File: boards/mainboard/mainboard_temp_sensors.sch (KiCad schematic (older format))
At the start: 1 part, among them J201 DB25_FEMALE

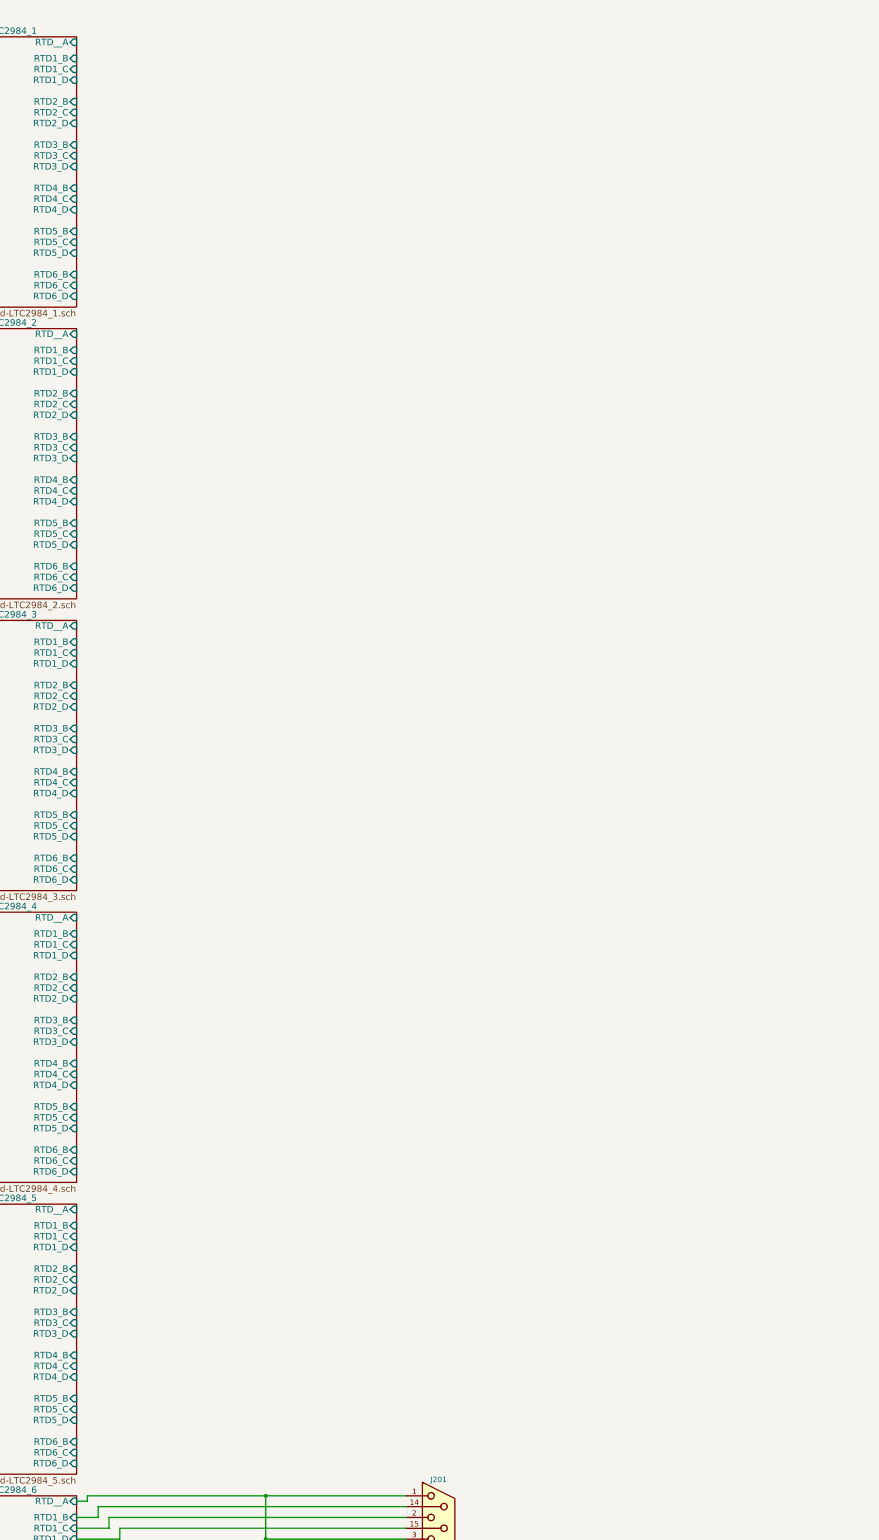
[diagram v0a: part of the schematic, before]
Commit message: [mainboard] add D-Sub HD 44 and 78 lib, wire PT-100 connectors
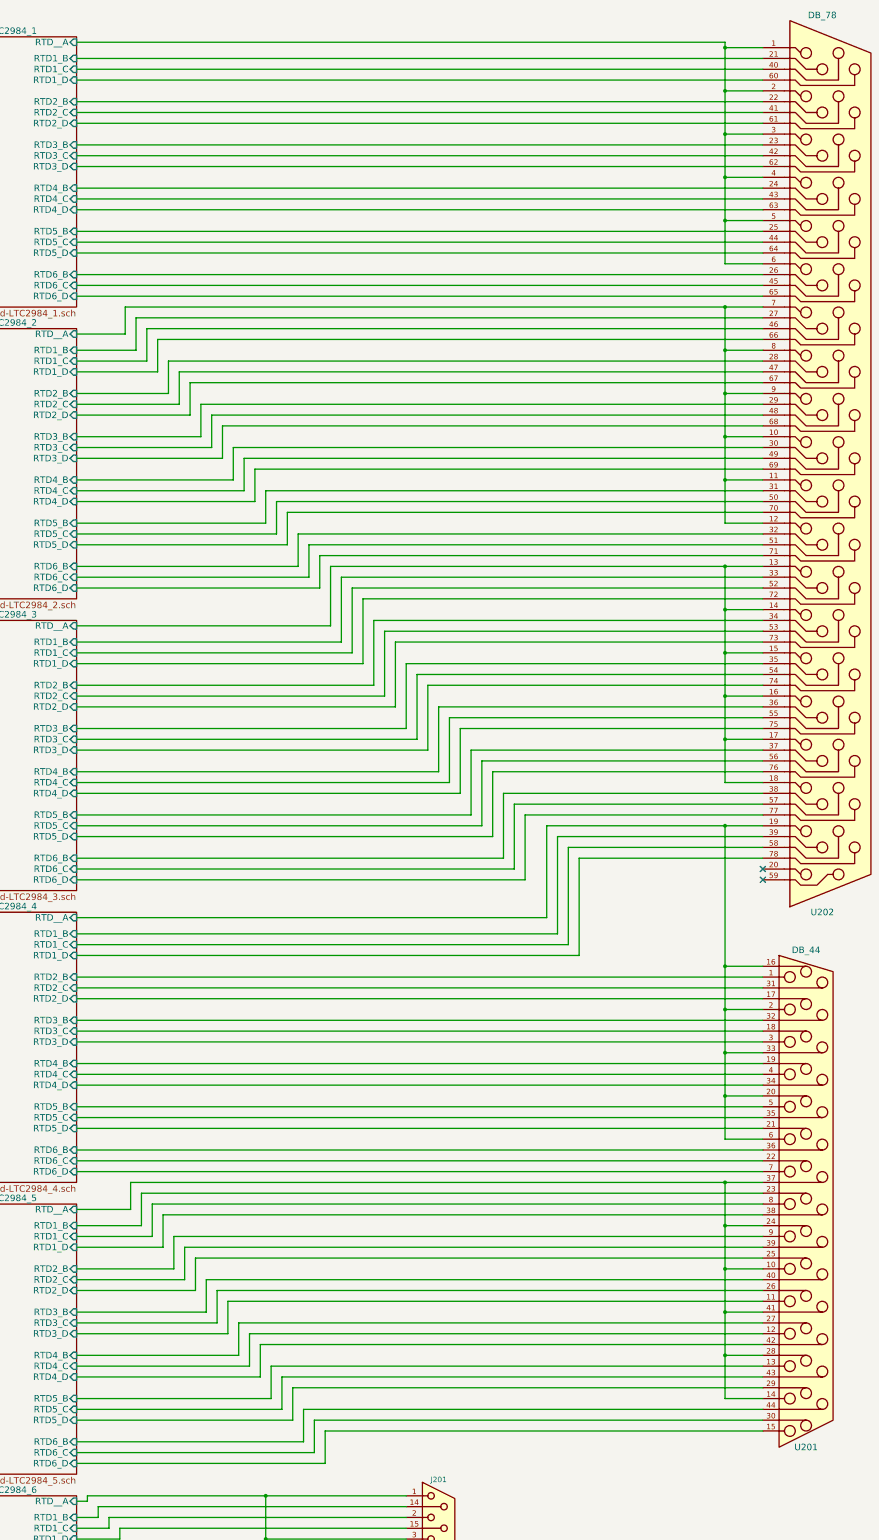
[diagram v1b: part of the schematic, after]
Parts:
- added U201: DB_44, symbol DB_44
- added U202: DB_78, symbol DB_78
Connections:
- net Mainboard_LTC2984_1/RTD1_B: now also U202.21
- net Mainboard_LTC2984_1/RTD1_C: now also U202.40
- net Mainboard_LTC2984_1/RTD1_D: now also U202.60
- net Mainboard_LTC2984_1/RTD2_B: now also U202.22
- net Mainboard_LTC2984_1/RTD2_C: now also U202.41
- net Mainboard_LTC2984_1/RTD2_D: now also U202.61
- net Mainboard_LTC2984_1/RTD3_B: now also U202.23
- net Mainboard_LTC2984_1/RTD3_C: now also U202.42
- net Mainboard_LTC2984_1/RTD3_D: now also U202.62
- net Mainboard_LTC2984_1/RTD4_B: now also U202.24
- net Mainboard_LTC2984_1/RTD4_C: now also U202.43
- net Mainboard_LTC2984_1/RTD4_D: now also U202.63
- net Mainboard_LTC2984_1/RTD5_B: now also U202.25
- net Mainboard_LTC2984_1/RTD5_C: now also U202.44
- net Mainboard_LTC2984_1/RTD5_D: now also U202.64
- net Mainboard_LTC2984_1/RTD6_B: now also U202.26
- net Mainboard_LTC2984_1/RTD6_C: now also U202.45
- net Mainboard_LTC2984_1/RTD6_D: now also U202.65
- net Mainboard_LTC2984_1/RTD__A: now also U202.1, U202.2, U202.3, U202.4, U202.5, U202.6
- net Mainboard_LTC2984_2/RTD1_B: now also U202.27
- net Mainboard_LTC2984_2/RTD1_C: now also U202.46
- net Mainboard_LTC2984_2/RTD1_D: now also U202.66
- net Mainboard_LTC2984_2/RTD2_B: now also U202.28
- net Mainboard_LTC2984_2/RTD2_C: now also U202.47
- net Mainboard_LTC2984_2/RTD2_D: now also U202.67
- net Mainboard_LTC2984_2/RTD3_B: now also U202.29
- net Mainboard_LTC2984_2/RTD3_C: now also U202.48
- net Mainboard_LTC2984_2/RTD3_D: now also U202.68
- net Mainboard_LTC2984_2/RTD4_B: now also U202.30
- net Mainboard_LTC2984_2/RTD4_C: now also U202.49
- net Mainboard_LTC2984_2/RTD4_D: now also U202.69
- net Mainboard_LTC2984_2/RTD5_B: now also U202.31
- net Mainboard_LTC2984_2/RTD5_C: now also U202.50
- net Mainboard_LTC2984_2/RTD5_D: now also U202.70
- net Mainboard_LTC2984_2/RTD6_B: now also U202.32
- net Mainboard_LTC2984_2/RTD6_C: now also U202.51
- net Mainboard_LTC2984_2/RTD6_D: now also U202.71
- net Mainboard_LTC2984_2/RTD__A: now also U202.10, U202.11, U202.12, U202.7, U202.8, U202.9
- net Mainboard_LTC2984_3/RTD1_B: now also U202.33
- net Mainboard_LTC2984_3/RTD1_C: now also U202.52
- net Mainboard_LTC2984_3/RTD1_D: now also U202.72
- net Mainboard_LTC2984_3/RTD2_B: now also U202.34
- net Mainboard_LTC2984_3/RTD2_C: now also U202.53
- net Mainboard_LTC2984_3/RTD2_D: now also U202.73
- net Mainboard_LTC2984_3/RTD3_B: now also U202.35
- net Mainboard_LTC2984_3/RTD3_C: now also U202.54
- net Mainboard_LTC2984_3/RTD3_D: now also U202.74
- net Mainboard_LTC2984_3/RTD4_B: now also U202.36
- net Mainboard_LTC2984_3/RTD4_C: now also U202.55
- net Mainboard_LTC2984_3/RTD4_D: now also U202.75
- net Mainboard_LTC2984_3/RTD5_B: now also U202.37
- net Mainboard_LTC2984_3/RTD5_C: now also U202.56
- net Mainboard_LTC2984_3/RTD5_D: now also U202.76
- net Mainboard_LTC2984_3/RTD6_B: now also U202.38
- net Mainboard_LTC2984_3/RTD6_C: now also U202.57
- net Mainboard_LTC2984_3/RTD6_D: now also U202.77
- net Mainboard_LTC2984_3/RTD__A: now also U202.13, U202.14, U202.15, U202.16, U202.17, U202.18
- net Mainboard_LTC2984_4/RTD1_B: now also U202.39
- net Mainboard_LTC2984_4/RTD1_C: now also U202.58
- net Mainboard_LTC2984_4/RTD1_D: now also U202.78
- net Mainboard_LTC2984_4/RTD2_B: now also U201.1
- net Mainboard_LTC2984_4/RTD2_C: now also U201.31
- net Mainboard_LTC2984_4/RTD2_D: now also U201.17
- net Mainboard_LTC2984_4/RTD3_B: now also U201.32
- net Mainboard_LTC2984_4/RTD3_C: now also U201.18
- net Mainboard_LTC2984_4/RTD3_D: now also U201.3
- net Mainboard_LTC2984_4/RTD4_B: now also U201.19
- net Mainboard_LTC2984_4/RTD4_C: now also U201.4
- net Mainboard_LTC2984_4/RTD4_D: now also U201.34
- net Mainboard_LTC2984_4/RTD5_B: now also U201.5
- net Mainboard_LTC2984_4/RTD5_C: now also U201.35
- net Mainboard_LTC2984_4/RTD5_D: now also U201.21
- net Mainboard_LTC2984_4/RTD6_B: now also U201.36
- net Mainboard_LTC2984_4/RTD6_C: now also U201.22
- net Mainboard_LTC2984_4/RTD6_D: now also U201.7
- net Mainboard_LTC2984_4/RTD__A: now also U201.16, U201.2, U201.20, U201.33, U201.6, U202.19
- net Mainboard_LTC2984_5/RTD1_B: now also U201.23
- net Mainboard_LTC2984_5/RTD1_C: now also U201.8
- net Mainboard_LTC2984_5/RTD1_D: now also U201.38
- net Mainboard_LTC2984_5/RTD2_B: now also U201.9
- net Mainboard_LTC2984_5/RTD2_C: now also U201.39
- net Mainboard_LTC2984_5/RTD2_D: now also U201.25
- net Mainboard_LTC2984_5/RTD3_B: now also U201.40
- net Mainboard_LTC2984_5/RTD3_C: now also U201.26
- net Mainboard_LTC2984_5/RTD3_D: now also U201.11
- net Mainboard_LTC2984_5/RTD4_B: now also U201.27
- net Mainboard_LTC2984_5/RTD4_C: now also U201.12
- net Mainboard_LTC2984_5/RTD4_D: now also U201.42
- net Mainboard_LTC2984_5/RTD5_B: now also U201.13
- net Mainboard_LTC2984_5/RTD5_C: now also U201.43
- net Mainboard_LTC2984_5/RTD5_D: now also U201.29
- net Mainboard_LTC2984_5/RTD6_B: now also U201.44
- net Mainboard_LTC2984_5/RTD6_C: now also U201.30
- net Mainboard_LTC2984_5/RTD6_D: now also U201.15
- net Mainboard_LTC2984_5/RTD__A: now also U201.10, U201.14, U201.24, U201.28, U201.37, U201.41
- no-connect marks 0 -> 2

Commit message: [mainboard] update connectors, select most footprints; docs: update SVGs
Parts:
- J201: value DB25_FEMALE -> RTD_31-36
- U201: value DB_44 -> RTD_20-30
- U202: value DB_78 -> RTD_1-19
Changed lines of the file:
@@
 Title "Mainboard Temperature Measurement Systems"
 Date "2017-04-19"
-Rev "11"
+Rev "12"
 Comp "VIPER"
 Comment1 ""
@@
 $EndSheet
 $Comp
-L DB25_FEMALE J201
-U 1 1 58FE1FD8
-P 7200 15600
-F 0 "J201" H 7200 16950 50  0000 C CNN
-F 1 "DB25_FEMALE" H 7200 14225 50  0000 C CNN
-F 2 "" H 7200 15600 50  0001 C CNN
-F 3 "" H 7200 15600 50  0001 C CNN
-	1    7200 15600
-	1    0    0    -1
-$EndComp
-$Comp
-L GND #PWR201
+L GND #PWR016
 U 1 1 58FE6256
 P 6800 16900
-F 0 "#PWR201" H 6800 16650 50  0001 C CNN
+F 0 "#PWR016" H 6800 16650 50  0001 C CNN
 F 1 "GND" H 6800 16750 50  0000 C CNN
 F 2 "" H 6800 16900 50  0001 C CNN
@@
 	1    0    0    -1
 $EndComp
-Wire Wire Line
-	6800 16900 6800 15600
-Wire Wire Line
-	6800 15600 6900 15600
-Wire Wire Line
-	3850 16800 6900 16800
-Wire Wire Line
-	3850 16700 6900 16700
-Wire Wire Line
-	3850 16600 6900 16600
-Wire Wire Line
-	3850 16400 6900 16400
-Wire Wire Line
-	3850 16300 6900 16300
-Wire Wire Line
-	6900 16200 3850 16200
-Wire Wire Line
-	3850 16000 6900 16000
-Wire Wire Line
-	6900 15900 3850 15900
-Wire Wire Line
-	3850 15800 6900 15800
-Wire Wire Line
-	3850 14600 4050 14600
-Wire Wire Line
-	4050 14600 4050 14500
-Wire Wire Line
-	4050 14500 6900 14500
-Wire Wire Line
-	6900 14600 4150 14600
-Wire Wire Line
-	4150 14600 4150 14700
-Wire Wire Line
-	4150 14700 3850 14700
-Wire Wire Line
-	3850 14800 4250 14800
-Wire Wire Line
-	4250 14800 4250 14700
-Wire Wire Line
-	4250 14700 6900 14700
-Wire Wire Line
-	6900 14900 4050 14900
-Wire Wire Line
-	4050 14900 4050 15000
-Wire Wire Line
-	4050 15000 3850 15000
-Wire Wire Line
-	3850 15100 4150 15100
-Wire Wire Line
-	4150 15100 4150 15000
-Wire Wire Line
-	4150 15000 6900 15000
-Wire Wire Line
-	6900 15100 4250 15100
-Wire Wire Line
-	4250 15100 4250 15200
-Wire Wire Line
-	4250 15200 3850 15200
-Wire Wire Line
-	3850 15400 4050 15400
-Wire Wire Line
-	4050 15400 4050 15300
-Wire Wire Line
-	4050 15300 6900 15300
-Wire Wire Line
-	6900 15400 4150 15400
-Wire Wire Line
-	4150 15400 4150 15500
-Wire Wire Line
-	4150 15500 3850 15500
-Wire Wire Line
-	3850 15600 4250 15600
-Wire Wire Line
-	4250 15600 4250 15500
-Wire Wire Line
-	4250 15500 6900 15500
-Wire Wire Line
-	3850 14450 3950 14450
-Wire Wire Line
-	3950 14450 3950 14400
-Wire Wire Line
-	3950 14400 6900 14400
-Wire Wire Line
-	5600 14400 5600 16500
-Wire Wire Line
-	5600 14800 6900 14800
-Connection ~ 5600 14400
-Wire Wire Line
-	5600 15200 6900 15200
-Connection ~ 5600 14800
-Wire Wire Line
-	5600 15700 6900 15700
-Connection ~ 5600 15200
-Wire Wire Line
-	5600 16100 6900 16100
-Connection ~ 5600 15700
-Wire Wire Line
-	5600 16500 6900 16500
-Connection ~ 5600 16100
-Wire Wire Line
-	1350 9200 2550 9200
-Wire Wire Line
-	1750 11900 2550 11900
-Connection ~ 1750 9200
-Wire Wire Line
-	1350 9300 2550 9300
-Wire Wire Line
-	2550 9400 1350 9400
-Wire Wire Line
-	1650 9300 1650 14700
-Wire Wire Line
-	1650 12000 2550 12000
-Connection ~ 1650 9300
-Wire Wire Line
-	2550 12100 1550 12100
-Wire Wire Line
-	1550 9400 1550 14800
-Connection ~ 1550 9400
-Wire Wire Line
-	1550 14800 2550 14800
-Connection ~ 1550 12100
-Wire Wire Line
-	1650 14700 2550 14700
-Connection ~ 1650 12000
-Wire Wire Line
-	1750 14600 2550 14600
-Connection ~ 1750 11900
-Wire Wire Line
-	2550 14500 2450 14500
-Wire Wire Line
-	2550 14900 2450 14900
-Wire Wire Line
-	2550 11800 2450 11800
-Wire Wire Line
-	2450 12200 2550 12200
-Wire Wire Line
-	1350 1100 2550 1100
-Wire Wire Line
-	2550 1200 1350 1200
-Wire Wire Line
-	1350 1300 2550 1300
-Wire Wire Line
-	2550 1400 2450 1400
-Wire Wire Line
-	2450 1000 2550 1000
-Wire Wire Line
-	1650 1200 1650 6600
-Wire Wire Line
-	1650 3900 2550 3900
-Connection ~ 1650 1200
-Wire Wire Line
-	2550 4000 1550 4000
-Wire Wire Line
-	1550 1300 1550 6700
-Connection ~ 1550 1300
-Wire Wire Line
-	1750 1100 1750 6500
-Wire Wire Line
-	1750 3800 2550 3800
-Connection ~ 1750 1100
-Wire Wire Line
-	2550 3700 2450 3700
-Wire Wire Line
-	2450 4100 2550 4100
-Wire Wire Line
-	1550 6700 2550 6700
-Connection ~ 1550 4000
-Wire Wire Line
-	1650 6600 2550 6600
-Connection ~ 1650 3900
-Wire Wire Line
-	1750 6500 2550 6500
-Connection ~ 1750 3800
-Wire Wire Line
-	2550 6400 2450 6400
-Wire Wire Line
-	2450 6800 2550 6800
-Wire Wire Line
-	2550 9500 2450 9500
-Wire Wire Line
-	2450 9100 2550 9100
-Wire Wire Line
-	1750 9200 1750 14600
 $Comp
 L DB_44 U201
@@
 P 10600 11600
 F 0 "U201" H 10600 9250 60  0000 C CNN
-F 1 "DB_44" H 10600 13850 60  0000 C CNN
+F 1 "RTD_20-30" H 10600 13850 60  0000 C CNN
 F 2 "" H 11800 11600 60  0001 C CNN
 F 3 "" H 11800 11600 60  0001 C CNN
@@
 P 10750 4700
 F 0 "U202" H 10750 400 60  0000 C CNN
-F 1 "DB_78" H 10750 8700 60  0000 C CNN
+F 1 "RTD_1-19" H 10750 8700 60  0000 C CNN
 F 2 "" H 10600 8400 60  0001 C CNN
 F 3 "" H 10600 8400 60  0001 C CNN
@@
 	1    0    0    -1
 $EndComp
+NoConn ~ 10200 8600
+NoConn ~ 10200 8700
+$Comp
+L DB25_FEMALE J201
+U 1 1 58FE1FD8
+P 7200 15600
+F 0 "J201" H 7200 16950 50  0000 C CNN
+F 1 "RTD_31-36" H 7200 14225 50  0000 C CNN
+F 2 "" H 7200 15600 50  0001 C CNN
+F 3 "" H 7200 15600 50  0001 C CNN
+	1    7200 15600
+	1    0    0    -1
+$EndComp
+Wire Wire Line
+	6800 16900 6800 15600
+Wire Wire Line
+	6800 15600 6900 15600
+Wire Wire Line
+	3850 16800 6900 16800
+Wire Wire Line
+	3850 16700 6900 16700
+Wire Wire Line
+	3850 16600 6900 16600
+Wire Wire Line
+	3850 16400 6900 16400
+Wire Wire Line
+	3850 16300 6900 16300
+Wire Wire Line
+	6900 16200 3850 16200
+Wire Wire Line
+	3850 16000 6900 16000
+Wire Wire Line
+	6900 15900 3850 15900
+Wire Wire Line
+	3850 15800 6900 15800
+Wire Wire Line
+	3850 14600 4050 14600
+Wire Wire Line
+	4050 14600 4050 14500
+Wire Wire Line
+	4050 14500 6900 14500
+Wire Wire Line
+	6900 14600 4150 14600
+Wire Wire Line
+	4150 14600 4150 14700
+Wire Wire Line
+	4150 14700 3850 14700
+Wire Wire Line
+	3850 14800 4250 14800
+Wire Wire Line
+	4250 14800 4250 14700
+Wire Wire Line
+	4250 14700 6900 14700
+Wire Wire Line
+	6900 14900 4050 14900
+Wire Wire Line
+	4050 14900 4050 15000
+Wire Wire Line
+	4050 15000 3850 15000
+Wire Wire Line
+	3850 15100 4150 15100
+Wire Wire Line
+	4150 15100 4150 15000
+Wire Wire Line
+	4150 15000 6900 15000
+Wire Wire Line
+	6900 15100 4250 15100
+Wire Wire Line
+	4250 15100 4250 15200
+Wire Wire Line
+	4250 15200 3850 15200
+Wire Wire Line
+	3850 15400 4050 15400
+Wire Wire Line
+	4050 15400 4050 15300
+Wire Wire Line
+	4050 15300 6900 15300
+Wire Wire Line
+	6900 15400 4150 15400
+Wire Wire Line
+	4150 15400 4150 15500
+Wire Wire Line
+	4150 15500 3850 15500
+Wire Wire Line
+	3850 15600 4250 15600
+Wire Wire Line
+	4250 15600 4250 15500
+Wire Wire Line
+	4250 15500 6900 15500
+Wire Wire Line
+	3850 14450 3950 14450
+Wire Wire Line
+	3950 14450 3950 14400
+Wire Wire Line
+	3950 14400 6900 14400
+Wire Wire Line
+	5600 14400 5600 16500
+Wire Wire Line
+	5600 14800 6900 14800
+Connection ~ 5600 14400
+Wire Wire Line
+	5600 15200 6900 15200
+Connection ~ 5600 14800
+Wire Wire Line
+	5600 15700 6900 15700
+Connection ~ 5600 15200
+Wire Wire Line
+	5600 16100 6900 16100
+Connection ~ 5600 15700
+Wire Wire Line
+	5600 16500 6900 16500
+Connection ~ 5600 16100
+Wire Wire Line
+	1350 9200 2550 9200
+Wire Wire Line
+	1750 11900 2550 11900
+Connection ~ 1750 9200
+Wire Wire Line
+	1350 9300 2550 9300
+Wire Wire Line
+	2550 9400 1350 9400
+Wire Wire Line
+	1650 9300 1650 14700
+Wire Wire Line
+	1650 12000 2550 12000
+Connection ~ 1650 9300
+Wire Wire Line
+	2550 12100 1550 12100
+Wire Wire Line
+	1550 9400 1550 14800
+Connection ~ 1550 9400
+Wire Wire Line
+	1550 14800 2550 14800
+Connection ~ 1550 12100
+Wire Wire Line
+	1650 14700 2550 14700
+Connection ~ 1650 12000
+Wire Wire Line
+	1750 14600 2550 14600
+Connection ~ 1750 11900
+Wire Wire Line
+	2550 14500 2450 14500
+Wire Wire Line
+	2550 14900 2450 14900
+Wire Wire Line
+	2550 11800 2450 11800
+Wire Wire Line
+	2450 12200 2550 12200
+Wire Wire Line
+	1350 1100 2550 1100
+Wire Wire Line
+	2550 1200 1350 1200
+Wire Wire Line
+	1350 1300 2550 1300
+Wire Wire Line
+	2550 1400 2450 1400
+Wire Wire Line
+	2450 1000 2550 1000
+Wire Wire Line
+	1650 1200 1650 6600
+Wire Wire Line
+	1650 3900 2550 3900
+Connection ~ 1650 1200
+Wire Wire Line
+	2550 4000 1550 4000
+Wire Wire Line
+	1550 1300 1550 6700
+Connection ~ 1550 1300
+Wire Wire Line
+	1750 1100 1750 6500
+Wire Wire Line
+	1750 3800 2550 3800
+Connection ~ 1750 1100
+Wire Wire Line
+	2550 3700 2450 3700
+Wire Wire Line
+	2450 4100 2550 4100
+Wire Wire Line
+	1550 6700 2550 6700
+Connection ~ 1550 4000
+Wire Wire Line
+	1650 6600 2550 6600
+Connection ~ 1650 3900
+Wire Wire Line
+	1750 6500 2550 6500
+Connection ~ 1750 3800
+Wire Wire Line
+	2550 6400 2450 6400
+Wire Wire Line
+	2450 6800 2550 6800
+Wire Wire Line
+	2550 9500 2450 9500
+Wire Wire Line
+	2450 9100 2550 9100
+Wire Wire Line
+	1750 9200 1750 14600
 Wire Wire Line
 	3850 1200 10200 1200
@@
 	9850 11900 10200 11900
 Connection ~ 9850 11900
-NoConn ~ 10200 8600
-NoConn ~ 10200 8700
 $EndSCHEMATC

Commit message: [mainboard] layout: footprints assigned, first placement
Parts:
- J201: footprint (none) -> Connectors:DB25FD
- U201: footprint (none) -> D-Sub-HD:D-Sub_HD_44_F
- U202: footprint (none) -> D-Sub-HD:D-Sub_HD_78_F
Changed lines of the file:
@@
 $EndSheet
 $Comp
-L GND #PWR016
+L GND #PWR014
 U 1 1 58FE6256
 P 6800 16900
-F 0 "#PWR016" H 6800 16650 50  0001 C CNN
+F 0 "#PWR014" H 6800 16650 50  0001 C CNN
 F 1 "GND" H 6800 16750 50  0000 C CNN
 F 2 "" H 6800 16900 50  0001 C CNN
@@
 F 0 "U201" H 10600 9250 60  0000 C CNN
 F 1 "RTD_20-30" H 10600 13850 60  0000 C CNN
-F 2 "" H 11800 11600 60  0001 C CNN
+F 2 "D-Sub-HD:D-Sub_HD_44_F" H 11800 11600 60  0001 C CNN
 F 3 "" H 11800 11600 60  0001 C CNN
 	1    10600 11600
@@
 F 0 "U202" H 10750 400 60  0000 C CNN
 F 1 "RTD_1-19" H 10750 8700 60  0000 C CNN
-F 2 "" H 10600 8400 60  0001 C CNN
+F 2 "D-Sub-HD:D-Sub_HD_78_F" H 10600 8400 60  0001 C CNN
 F 3 "" H 10600 8400 60  0001 C CNN
 	1    10750 4700
@@
 F 0 "J201" H 7200 16950 50  0000 C CNN
 F 1 "RTD_31-36" H 7200 14225 50  0000 C CNN
-F 2 "" H 7200 15600 50  0001 C CNN
+F 2 "Connectors:DB25FD" H 7200 15600 50  0001 C CNN
 F 3 "" H 7200 15600 50  0001 C CNN
 	1    7200 15600
